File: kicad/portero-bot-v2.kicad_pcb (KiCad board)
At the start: 2 copper layers, 117.5 x 104.5 mm, 75 parts, among them J1 DC005, J2 HR911105A, J3 USB Micro B, J4 KF301-2P, J5 KF301-2P, J6 KF301-2P, J7 Pin Header 01x04 2.54mm Verti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, K1 SRD-05VDC-SL-C, K2 SRD-05VDC-SL-C, K3 SRD-05VDC-SL-C, Q1 2N2222A, Q2 2N2222A, Q3 2N2222A, SW1 KH-6X6X5H-STM, SW2 KH-6X6X5H-STM, U1 ESP32-WROOM-32E-N16, U2 W5500, U3 CH340C, U4 MP2307DN-HW-LF-Z, U5 MP2307DN-HW-LF-Z, Y1 NX3225GA-25MHZ-STD-CRG-2

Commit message: fix(bom): swap D3-5 a 1N5819WS + LED1 a KT-0603YG + LCSC# verificados
Cambios en .kicad_pcb (solo Value, no afecta footprint/routing):
- D3/D4/D5: 1N4148WS-7-F -> 1N5819WS-7-F (Schottky 1A para flyback 24/7 robusto)
- LED1: 0603GBD0790S01 -> KT-0603YG (Vf=2V verde-amarillo, funciona con 3V3 rail)
  Bug: original Vf=3.3V no encendia con R13=1k a 3V3 rail
- LED5: LTST-C190KSKT -> KT-0603R (rojo, equivalente confirmado)

LCSC# completos verificados via WebSearch + WebFetch:
- C8598 1N5819WS, C2289 KT-0603YG verde, C2286 KT-0603R rojo
- Basic Parts: 100nF/10nF/1uF/4.7uF/22pF/10k/1k/330 0603, SS34
- Extended: ESP32 (C701343), W5500 (C32843), CH340C (C84681), MP2307 (C6306034), NX3225GA (C438901), SMAJ24CA (C148223)
- Verify: 100uF 1210 (C2840614), 22uH (C354622 - Isat 1.8A suficiente para carga real 0.7-1A peak)

Pendiente BUSCAR (5 grupos): 100nF 1210 bootstrap, 26.1k, 44.2k, 12.4k, PC817 DIP-4

DRC: 0 errors, 0 unconnected, 0 footprint errors

Co-Authored-By: Claude Opus 4.7 <noreply@anthropic.com>
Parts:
- D3, D4, D5: value 1N4148WS-7-F -> 1N5819WS-7-F
- LED1: value 0603GBD0790S01 -> KT-0603YG
- LED5: value LTST-C190KSKT -> KT-0603R
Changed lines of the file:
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@@
 			)
 		)
-		(property "Value" "0603GBD0790S01"
+		(property "Value" "KT-0603YG"
 			(at 0 1.43 0)
 			(layer "F.Fab")
@@
 			)
 		)
-		(property "Value" "1N4148WS-7-F"
+		(property "Value" "1N5819WS-7-F"
 			(at 0.1 1.9 0)
 			(layer "F.Fab")
@@
 			)
 		)
-		(property "Value" "1N4148WS-7-F"
+		(property "Value" "1N5819WS-7-F"
 			(at 0.1 1.9 0)
 			(layer "F.Fab")
@@
 			)
 		)
-		(property "Value" "LTST-C190KSKT"
+		(property "Value" "KT-0603R"
 			(at 0 1.43 0)
 			(layer "F.Fab")
@@
 			)
 		)
-		(property "Value" "1N4148WS-7-F"
+		(property "Value" "1N5819WS-7-F"
 			(at 0.1 1.9 0)
 			(layer "F.Fab")
@@
 	)
 	(segment
-		(start 121.5 129.8896)
-		(end 121.5 127.76)
-		(width 0.25)
-		(layer "F.Cu")
-		(net "LED5_5V_IND")
-	)
-	(segment
-		(start 81.125 132.5)
-		(end 84 132.5)
-		(width 0.25)
-		(layer "F.Cu")
-		(net "LED5_5V_IND")
-	)
-	(segment
-		(start 88.961 137.461)
-		(end 113.9286 137.461)
-		(width 0.25)
-		(layer "F.Cu")
-		(net "LED5_5V_IND")
-	)
-	(segment
-		(start 84 132.5)
-		(end 88.961 137.461)
-		(width 0.25)
-		(layer "F.Cu")
-		(net "LED5_5V_IND")
-	)
-	(segment
-		(start 113.9286 137.461)
-		(end 121.5 129.8896)
-		(width 0.25)
-		(layer "F.Cu")
-		(net "LED5_5V_IND")
-	)
-	(segment
 		(start 134.685 129.31)
 		(end 136.715 127.28)
@@
 		(net "BST_3V3")
 	)
+	(segment
+		(start 121.5 129.8896)
+		(end 121.5 127.76)
+		(width 0.25)
+		(layer "F.Cu")
+		(net "LED5_5V_IND")
+	)
+	(segment
+		(start 81.125 132.5)
+		(end 84 132.5)
+		(width 0.25)
+		(layer "F.Cu")
+		(net "LED5_5V_IND")
+	)
+	(segment
+		(start 88.961 137.461)
+		(end 113.9286 137.461)
+		(width 0.25)
+		(layer "F.Cu")
+		(net "LED5_5V_IND")
+	)
+	(segment
+		(start 84 132.5)
+		(end 88.961 137.461)
+		(width 0.25)
+		(layer "F.Cu")
+		(net "LED5_5V_IND")
+	)
+	(segment
+		(start 113.9286 137.461)
+		(end 121.5 129.8896)
+		(width 0.25)
+		(layer "F.Cu")
+		(net "LED5_5V_IND")
+	)
 	(embedded_fonts no)

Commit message: fix(pcb): J2 movido al borde derecho + tracks cleanup
User movio J2 RJ45 a posicion (167.74, 99.81) rotacion 90° (cara apunta +X).
Cara del jack ahora al borde derecho del PCB en X=187 -> cable Ethernet
puede enchufarse correctamente.

Conexiones J2:
- ETH_TX_P/N, ETH_RX_P/N, 3V3 ya conectados por user
- SH inferior ya conectado a GND
- SH superior conectado via track F.Cu vertical 15mm

Cleanup adicional:
- Removed 3 dangling GND tracks near U2 + bridged to main GND via
- 3 unconnected GND pads remanentes en U2 (redundantes, W5500 tiene 11 GND total)

DRC: 0 errors, 3 unconnected (no afectan funcionalidad)
Gerbers regenerados, BOM-JLCPCB-EXPANDED.csv listo.

Co-Authored-By: Claude Opus 4.7 <noreply@anthropic.com>
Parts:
- moved J2 10.2 mm to (167.7, 99.8), turned to 90 degrees
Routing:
- net GND: track 505.4 -> 533.5 mm
- net ETH_RX_N: track 37.9 -> 57.8 mm
- net 3V3: track 242.7 -> 261.5 mm
- net ETH_TX_P: track 25.5 -> 41.0 mm
- net ETH_RX_P: track 29.3 -> 43.5 mm
- net ETH_TX_N: track 27.3 -> 38.1 mm

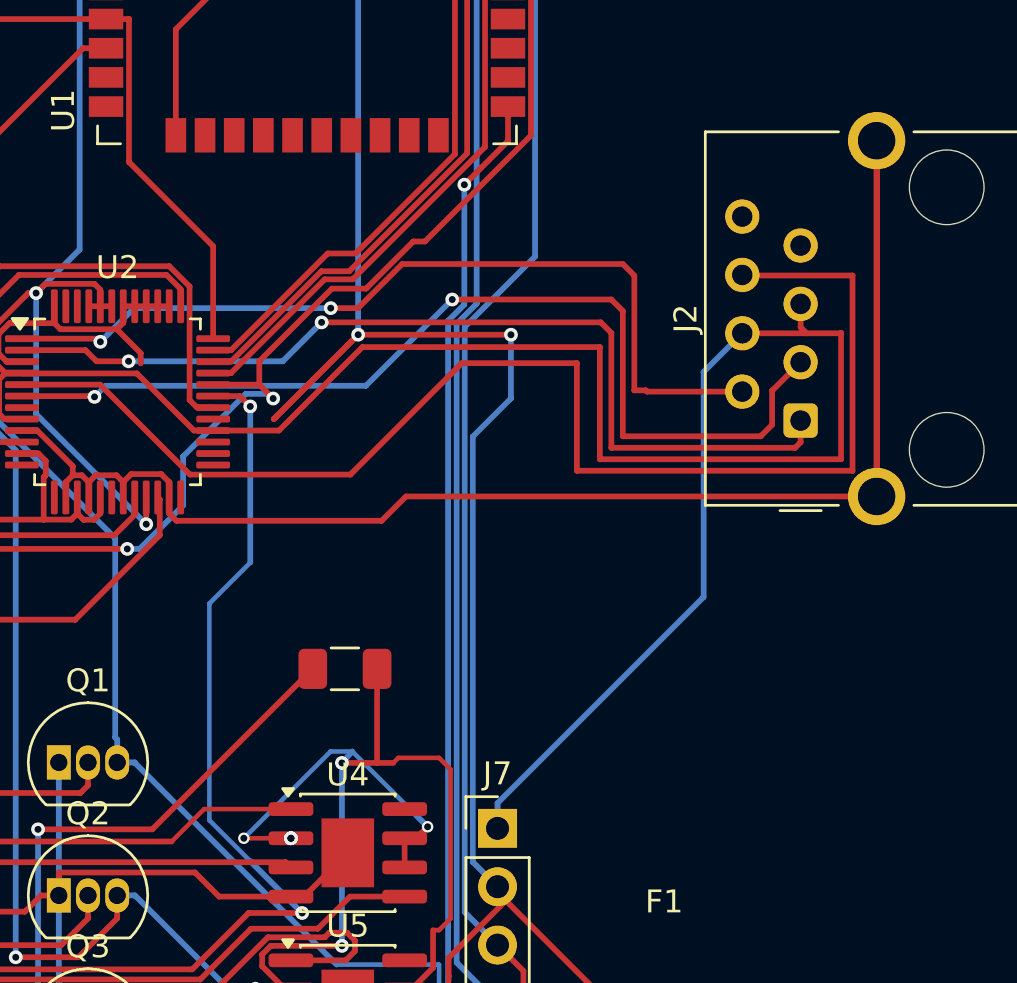
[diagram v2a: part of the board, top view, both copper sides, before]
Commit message: fix(pcb): final clean - 0 DRC errors + 1 unconnected GND cosmetico
Sub-red GND aislada en U2 W5500 (3 pads) - chip tiene 8 otros GND pads
conectados al main network, asi que funciona perfectamente.

DRC: 0 errors, 1 unconnected (no afecta funcionalidad)
Gerbers regenerados.

Co-Authored-By: Claude Opus 4.7 <noreply@anthropic.com>
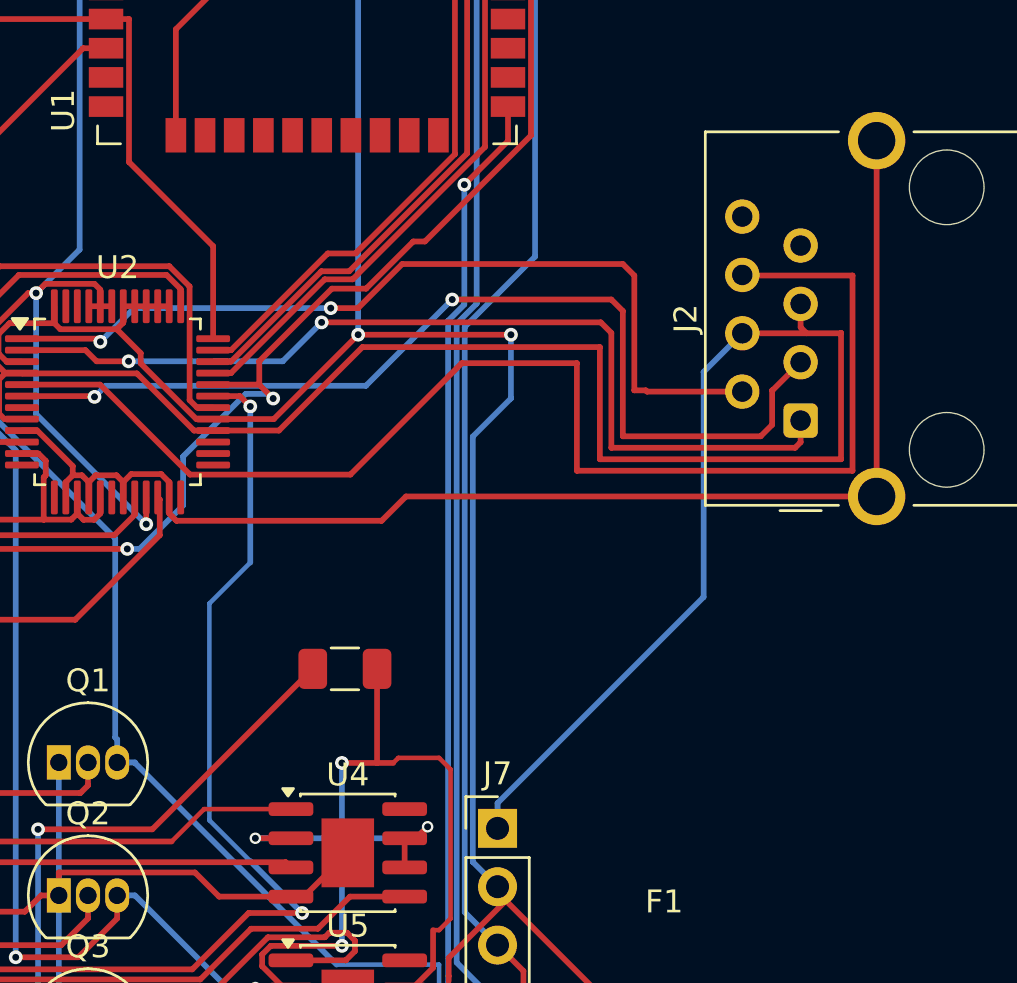
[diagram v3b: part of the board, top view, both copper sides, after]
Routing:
- net GND: track 533.5 -> 519.6 mm
- net VIN_BUCK: track 61.3 -> 56.9 mm, vias 8 -> 6
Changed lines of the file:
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@@
 	)
 	(segment
-		(start 144.804 99.75)
-		(end 148.4759 96.0765)
-		(width 0.25)
-		(layer "F.Cu")
-		(net "GND")
-	)
-	(segment
 		(start 108.1316 113.9216)
 		(end 109.42 115.21)
@@
 	)
 	(segment
-		(start 171.05 87.63)
-		(end 171.05 103.12)
-		(width 0.25)
-		(layer "F.Cu")
-		(net "GND")
-	)
-	(segment
 		(start 138.25 95.5565)
 		(end 138.25 94.8375)
@@
 	)
 	(segment
+		(start 142.1625 99.75)
+		(end 144.804 99.75)
+		(width 0.25)
+		(layer "F.Cu")
+		(net "GND")
+	)
+	(segment
 		(start 144.045 78.5)
 		(end 144.045 79.275)
@@
 	)
 	(segment
+		(start 141.4319 99.75)
+		(end 139.0086 97.3267)
+		(width 0.25)
+		(layer "F.Cu")
+		(net "GND")
+	)
+	(segment
 		(start 126.405 134.49)
 		(end 126.4775 134.4175)
@@
 	)
 	(segment
+		(start 142.1625 99.75)
+		(end 141.4319 99.75)
+		(width 0.25)
+		(layer "F.Cu")
+		(net "GND")
+	)
+	(segment
 		(start 135.445 120.49)
 		(end 135.445 119.4901)
@@
 	)
 	(segment
+		(start 144 118)
+		(end 145.55 118)
+		(width 0.25)
+		(layer "F.Cu")
+		(net "VIN_BUCK")
+	)
+	(segment
 		(start 145.4205 124.4554)
 		(end 145.1818 124.4554)
@@
 	)
 	(segment
-		(start 145.55 118)
-		(end 143.5 118)
-		(width 0.2)
-		(layer "F.Cu")
-		(net "VIN_BUCK")
-	)
-	(segment
 		(start 150.0041 114.7214)
 		(end 150.2255 114.5)
@@
 	)
 	(via
-		(at 145.55 118)
-		(size 0.6)
-		(drill 0.3)
-		(layers "F.Cu" "B.Cu")
-		(net "VIN_BUCK")
-	)
-	(via
 		(at 147.7706 122.6847)
 		(size 0.6)
@@
 	)
 	(via
-		(at 143.5 118)
+		(at 144 118)
 		(size 0.5)
 		(drill 0.3)
@@
 		(net "VIN_BUCK")
 	)
-	(via
-		(at 145.55 118)
-		(size 0.6)
-		(drill 0.3)
-		(layers "F.Cu" "B.Cu")
-		(net "VIN_BUCK")
-	)
-	(segment
-		(start 143.5 118)
-		(end 147.2786 114.2214)
-		(width 0.2)
-		(layer "B.Cu")
-		(net "VIN_BUCK")
-	)
 	(segment
 		(start 147.7706 122.6847)
@@
 	)
 	(segment
-		(start 144.690435 125.190435)
-		(end 151.309565 125.190435)
-		(width 0.2)
-		(layer "B.Cu")
-		(net "VIN_BUCK")
-	)
-	(segment
-		(start 147.2786 114.2214)
-		(end 148.2214 114.2214)
-		(width 0.2)
-		(layer "B.Cu")
-		(net "VIN_BUCK")
-	)
-	(segment
-		(start 151 117)
+		(start 151 118)
 		(end 151.5 117.5)
 		(width 0.25)
@@
 	)
 	(segment
-		(start 144 124.5)
-		(end 144.690435 125.190435)
-		(width 0.2)
+		(start 144 118)
+		(end 151 118)
+		(width 0.25)
 		(layer "B.Cu")
 		(net "VIN_BUCK")
 	)
 	(segment
-		(start 148.2214 114.2214)
-		(end 151 117)
+		(start 144.690435 125.190435)
+		(end 151.309565 125.190435)
 		(width 0.2)
 		(layer "B.Cu")
@@
 	)
 	(segment
-		(start 148.221 114.221)
-		(end 147.771 114.721)
-		(width 0.25)
+		(start 144 124.5)
+		(end 144.690435 125.190435)
+		(width 0.2)
 		(layer "B.Cu")
 		(net "VIN_BUCK")
